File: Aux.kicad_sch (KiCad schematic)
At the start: 23 parts, among them J3 Molex_39281143, P11 CHARGE_A22, P14 SPARE_IGN6, P15 SPARE_IGN7, P16 SPARE_IGN8, P17 I2C_1_SCL, P18 I2C_1_SDA, P19 +5VA, P20 +3.3V, P21 +12V_RAW, P22 GND, P27 SPARE_PWM3, P28 SPARE_RES2, P29 AUX_IN1, P30 AUX_IN2, P31 AUX_IN3

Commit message: U1 is the library USBLC6-2SC6 (EE-C-0146); J2 part numbers; test pads and proto area out of the BOM
- U1 used the USBLC6-2P6 (SOT-666) symbol with a hand-changed footprint; now EmbeddedEra:USBLC6-2SC6.
- J2 instance had no Manufacturer/MPN although the library has them.
- P1-P32 and G1 are pads, nothing is bought (SOP-008 step 18): in_bom no, as in the library.

Co-Authored-By: Claude Opus 5.5 <noreply@anthropic.com>
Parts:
- G1, P11, P14, P15, P16, P17, P18, P19, P20, P21, P22, P27, P28, P29, P30, P31: now left out of the parts list
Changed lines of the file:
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@@
 		(body_style 1)
 		(exclude_from_sim no)
-		(in_bom yes)
+		(in_bom no)
 		(on_board yes)
 		(in_pos_files yes)
@@
 		(body_style 1)
 		(exclude_from_sim no)
-		(in_bom yes)
+		(in_bom no)
 		(on_board yes)
 		(in_pos_files yes)
@@
 		(body_style 1)
 		(exclude_from_sim no)
-		(in_bom yes)
+		(in_bom no)
 		(on_board yes)
 		(in_pos_files yes)
@@
 		(body_style 1)
 		(exclude_from_sim no)
-		(in_bom yes)
+		(in_bom no)
 		(on_board yes)
 		(in_pos_files yes)
@@
 		(body_style 1)
 		(exclude_from_sim no)
-		(in_bom yes)
+		(in_bom no)
 		(on_board yes)
 		(in_pos_files yes)
@@
 		(body_style 1)
 		(exclude_from_sim no)
-		(in_bom yes)
+		(in_bom no)
 		(on_board yes)
 		(in_pos_files yes)
@@
 		(body_style 1)
 		(exclude_from_sim no)
-		(in_bom yes)
+		(in_bom no)
 		(on_board yes)
 		(in_pos_files yes)
@@
 		(body_style 1)
 		(exclude_from_sim no)
-		(in_bom yes)
+		(in_bom no)
 		(on_board yes)
 		(in_pos_files yes)
@@
 		(body_style 1)
 		(exclude_from_sim no)
-		(in_bom yes)
+		(in_bom no)
 		(on_board yes)
 		(in_pos_files yes)
@@
 		(body_style 1)
 		(exclude_from_sim no)
-		(in_bom yes)
+		(in_bom no)
 		(on_board yes)
 		(in_pos_files yes)
@@
 		(body_style 1)
 		(exclude_from_sim no)
-		(in_bom yes)
+		(in_bom no)
 		(on_board yes)
 		(in_pos_files yes)
@@
 		(body_style 1)
 		(exclude_from_sim no)
-		(in_bom yes)
+		(in_bom no)
 		(on_board yes)
 		(in_pos_files yes)
@@
 		(body_style 1)
 		(exclude_from_sim no)
-		(in_bom yes)
+		(in_bom no)
 		(on_board yes)
 		(in_pos_files yes)
@@
 		(body_style 1)
 		(exclude_from_sim no)
-		(in_bom yes)
+		(in_bom no)
 		(on_board yes)
 		(in_pos_files yes)
@@
 		(body_style 1)
 		(exclude_from_sim no)
-		(in_bom yes)
+		(in_bom no)
 		(on_board yes)
 		(in_pos_files yes)
@@
 		(body_style 1)
 		(exclude_from_sim no)
-		(in_bom yes)
+		(in_bom no)
 		(on_board yes)
 		(in_pos_files yes)

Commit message: Title block: TITLE is the project name (${Project_Name}) on every sheet, DESCRIPTION the sheet name
The LS/INJ sub-sheet and the root had no title at all.

Co-Authored-By: Claude Opus 5.5 <noreply@anthropic.com>
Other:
- title: Aux and expansion -> ${Project_Name}
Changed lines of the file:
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@@
 	(paper "A3")
 	(title_block
-		(title "Aux and expansion")
+		(title "${Project_Name}")
 		(date "2026-10-13")
 	)

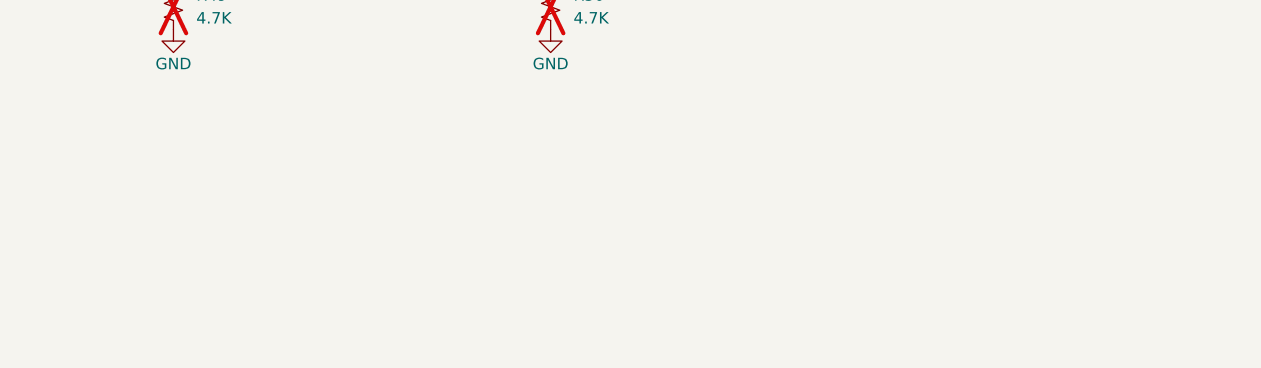
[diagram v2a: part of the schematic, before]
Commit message: PCB: update from schematic and first placement; H1-H4 M3 mounting holes; drop STI.pretty
- kicad-pcb-from-netlist (EmbeddedEra/KiCad scripting/pcb) rebuilt the rev-a board: 137 footprints,
  linked to their symbols (DRC schematic parity 0), nets on every pad, floorplan in pcb_place.json.
- H1-H4 added to the schematic (Aux sheet) first, then placed.
- STI.pretty removed: the board now uses EmbeddedEra_Library:TE_1-1376430-0.
- hellen-create-board builds the full package again (the F5 mismatch is gone).

Co-Authored-By: Claude Opus 5.5 <noreply@anthropic.com>
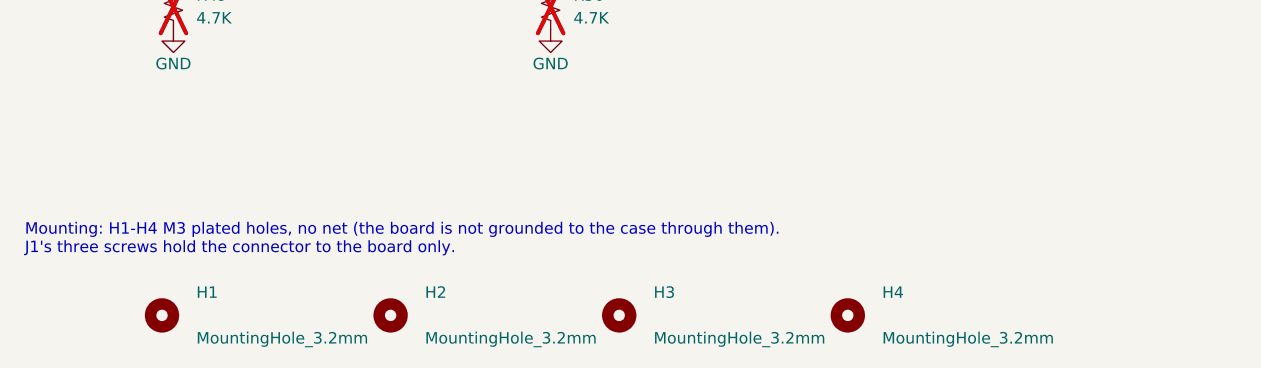
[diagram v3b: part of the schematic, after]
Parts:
- added H1, H2, H3, H4: MountingHole_3.2mm, EmbeddedEra_Library:MountingHole_3.2mm_M3_DIN965_Pad, symbol EmbeddedEra:MountingHole_3.2mm
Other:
- note added: "Mounting: H1-H4 M3 plated holes, no net (the board is not grounded to the case through them). J1's three screws hold the connector to the board only."

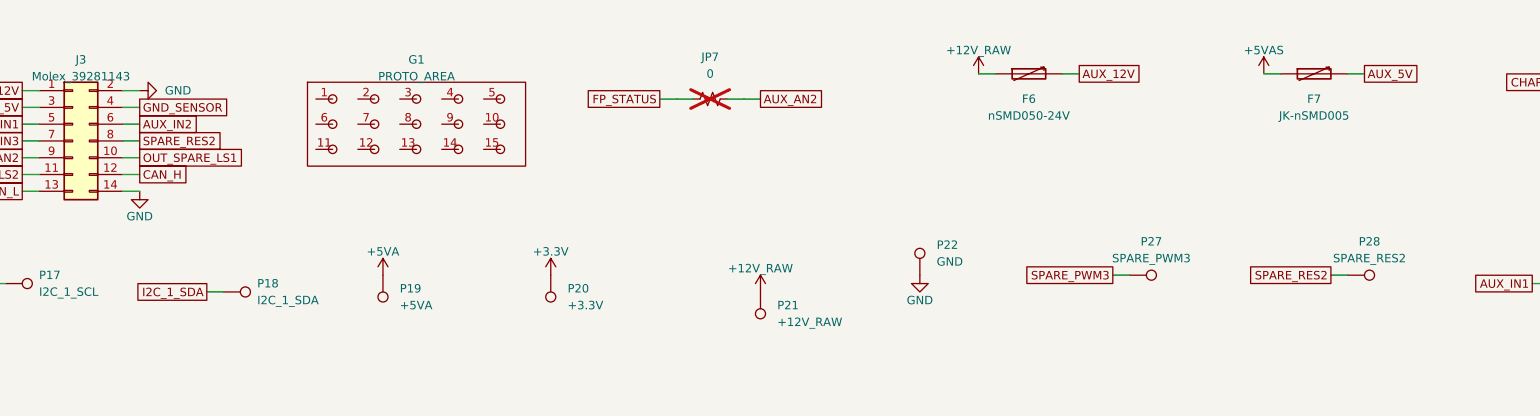
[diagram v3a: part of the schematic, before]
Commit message: On-board MAP sensor (AlphaX style): U20 MPXHZ6400AC6T1 + C1 100n on +5VA -> M1 IN_MAP3 (S19)
TGV position RH moves from IN_MAP3 to IN_RES2 (S14). J3 pin 8 (was AUX_AN1 on
IN_RES2) is now not connected; P28 is the MAP test pad. External MAP stays on
IN_MAP1. PCB: U20/C1 placed left of M1, DRC 0 errors, unconnected 322.

Co-Authored-By: Claude Opus 5.5 <noreply@anthropic.com>
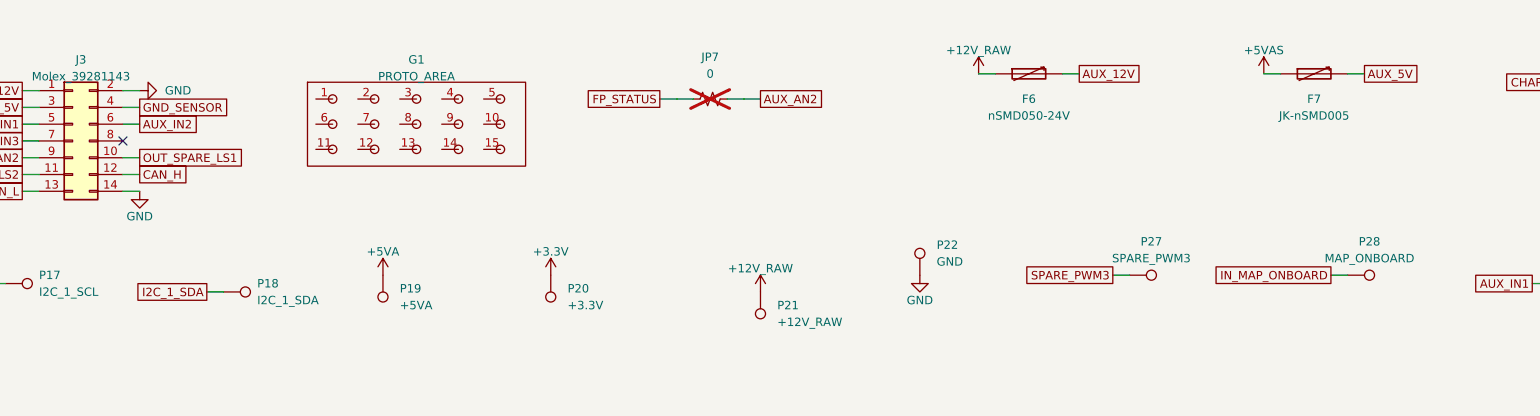
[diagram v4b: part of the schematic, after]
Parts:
- P28: value SPARE_RES2 -> MAP_ONBOARD
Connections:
- net SPARE_RES2: no longer names the net of J3.8 (Pin_8)
- net SPARE_RES2: no longer P28.1
- new net IN_MAP_ONBOARD: P28.1
- no-connect marks 0 -> 1
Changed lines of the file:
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@@
 		)
 	)
-	(wire
-		(pts
-			(xy 49.53 54.61) (xy 52.07 54.61)
-		)
-		(stroke
-			(width 0)
-			(type default)
-		)
+	(no_connect
+		(at 49.53 54.61)
 	)
 	(wire
@@
 		)
 	)
-	(global_label "SPARE_RES2"
-		(shape passive)
-		(at 52.07 54.61 0)
-		(fields_autoplaced yes)
-		(effects
-			(font
-				(size 1.27 1.27)
-			)
-			(justify left)
-		)
-		(property "Intersheetrefs" "${INTERSHEET_REFS}"
-			(at 52.07 54.61 0)
-			(hide yes)
-			(show_name no)
-			(do_not_autoplace no)
-			(effects
-				(font
-					(size 1.27 1.27)
-				)
-				(justify left)
-			)
-		)
-	)
 	(global_label "OUT_SPARE_LS1"
 		(shape passive)
@@
 		)
 	)
-	(global_label "SPARE_RES2"
+	(global_label "IN_MAP_ONBOARD"
 		(shape passive)
 		(at 232.41 74.93 180)
@@
 			)
 		)
-		(property "Value" "SPARE_RES2"
+		(property "Value" "MAP_ONBOARD"
 			(at 238.252 72.39 90)
 			(show_name no)
